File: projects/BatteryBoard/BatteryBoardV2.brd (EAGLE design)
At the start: 86.8 x 90.4 mm, 187 parts, among them M1 BSO201SP, SW1 BTS50015-1TAD, SW2 BTS50015-1TAD, U1 LTC4412MPS6, U3 LTC4121-4.2, U4 LTC4121-4.2, U5 LTC4121, U6 LTC4121

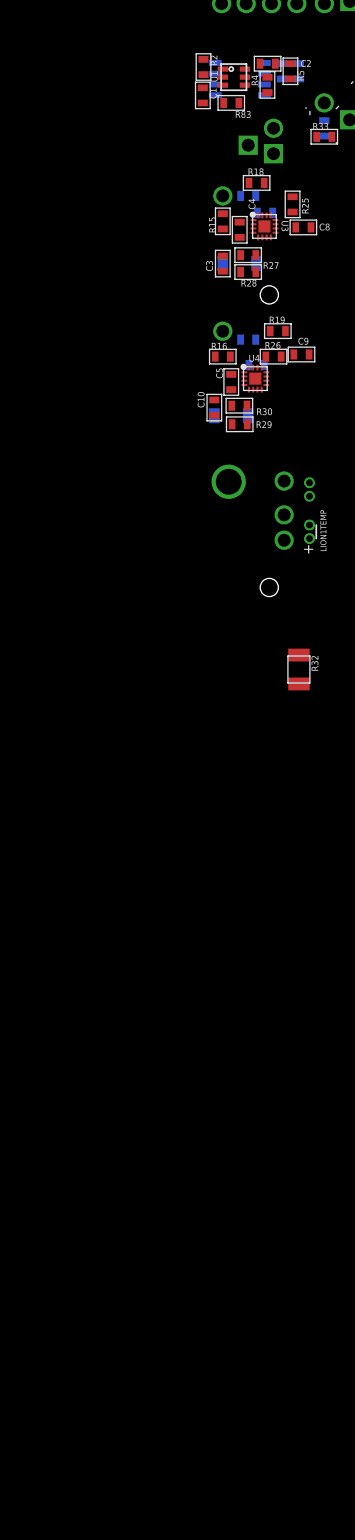
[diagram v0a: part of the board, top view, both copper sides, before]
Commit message: Finished programmer board and added output files to repo. Addiong of LDOs and continued fixes and updates to battery board v2.
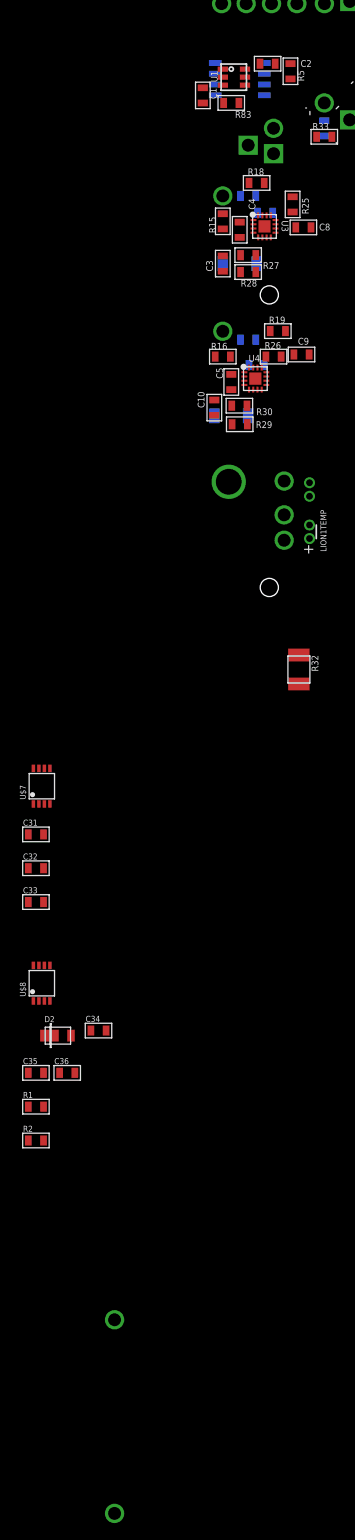
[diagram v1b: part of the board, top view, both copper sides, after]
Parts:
- removed R11: 10R, BrownSpaceEngineering:0805
- removed R12, R4: 0R, BrownSpaceEngineering:0805
- added C31, C34: 10uF, BrownSpaceEngineering:0805
- added C32, C35: 0.01uF, BrownSpaceEngineering:0805
- added C33, C36: 1uF, BrownSpaceEngineering:0805
- added D2: DFLS130L, BrownSpaceEngineering:PWRDI-123
- added R1: 1M, BrownSpaceEngineering:0805
- added U$7, U$8: LT1962-3, BrownSpaceEngineering:MSOP-8
- added V7, V8: (no value), BrownSpaceEngineering:VIA-60MIL
- D1: value (none) -> DFLS130L
- R2: value 0R -> 1M
- R84: value 1K -> 10K
- moved R2 128.5 mm to (-116.5, -63.4), turned to 0 degrees
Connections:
- removed net SP_C_O: R11.1, R12.1, R4.2, R5.2
- new net N$14: R2.2, U4.P$11
- new net N$3: C34.1, C35.1, D2.A, U$8.P$1, U$8.P$2
- new net N$4: C32.2, U$7.P$3
- new net N$6: R1.2, U3.P$11
- net GND: now also C31.2, C33.2, C34.2, C36.2, R1.1, R2.1, U$7.P$4, U$7.P$6, U$7.P$7, U$8.P$4, U$8.P$6, U$8.P$7; no longer R31.P$1
- net L_OUT: now also D1.C, D2.C
- net N$2: now also C31.1, C32.1, D1.A, U$7.P$1, U$7.P$2; no longer C2.1, M1.P$1, M1.P$2, M1.P$3, R4.1, U1.P$6
- net N$5: now also C35.2, U$8.P$3; no longer C1.1, M1.P$5, M1.P$6, M1.P$7, M1.P$8, R2.2, U1.P$1
- net SP_C: now also C1.1, M1.P$5, M1.P$6, M1.P$7, M1.P$8, U1.P$1; no longer R2.1
- net SP_OUT: now also C2.1, C33.1, C36.1, M1.P$1, M1.P$2, M1.P$3, R5.2, U$7.P$5, U$7.P$8, U$8.P$5, U$8.P$8, U1.P$6; no longer R11.2, R12.2

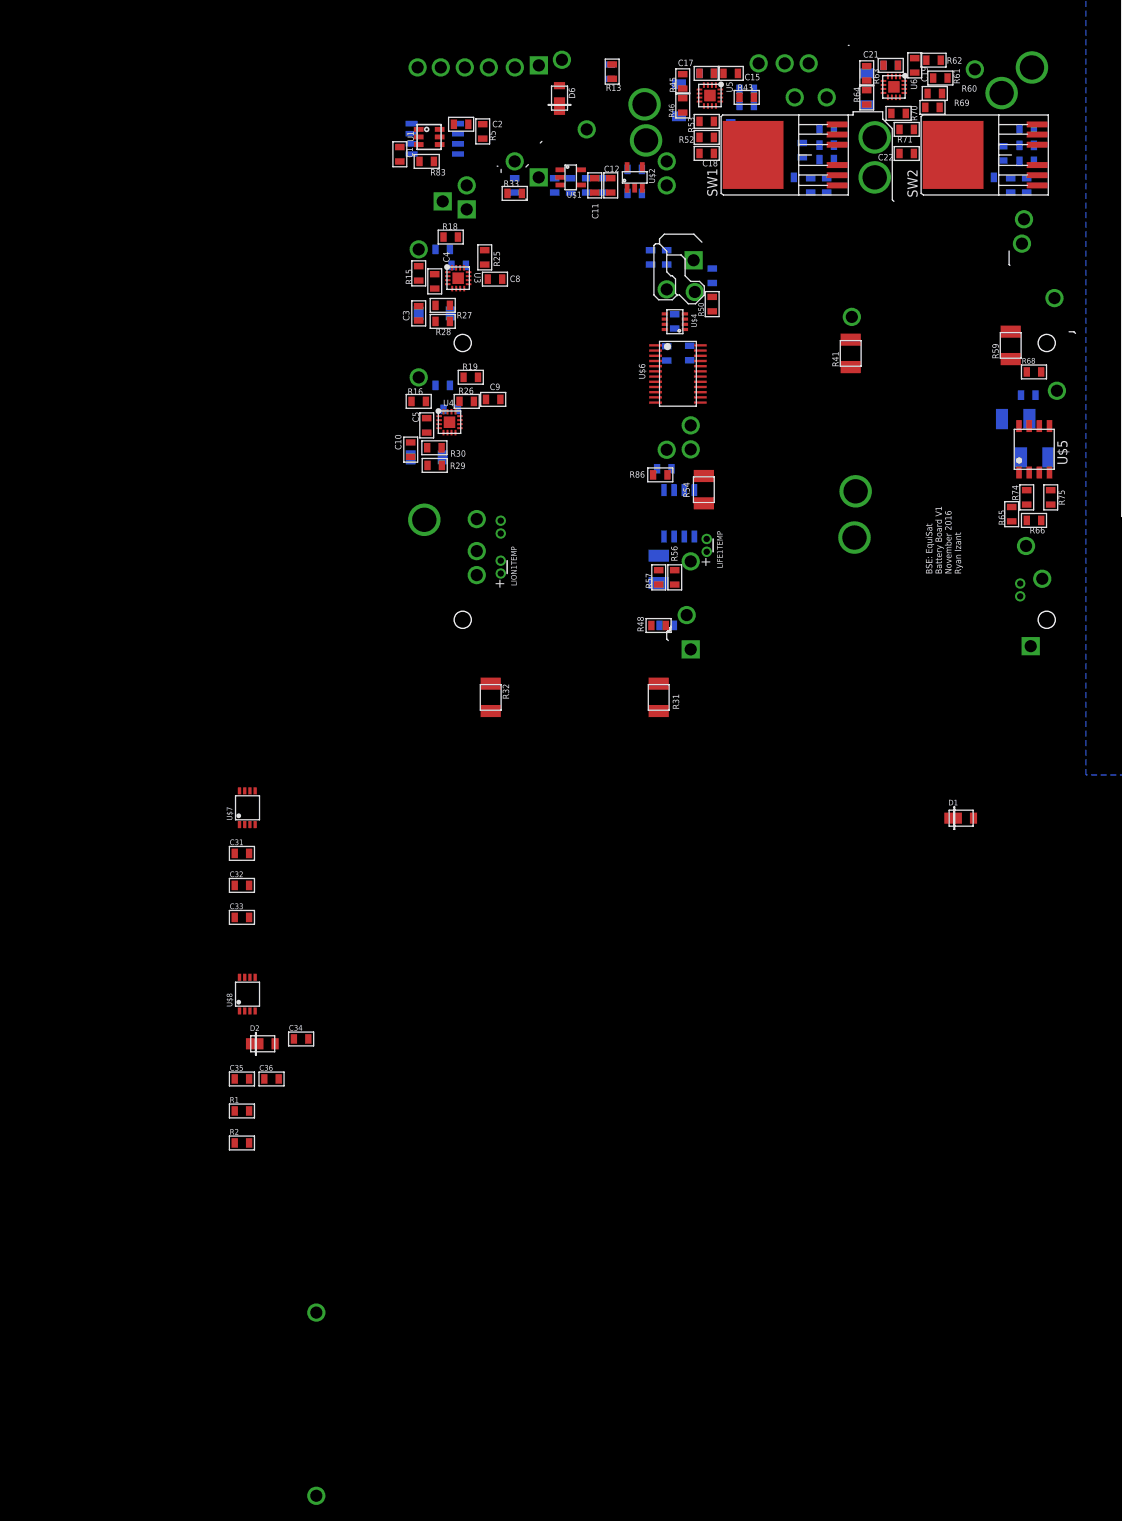
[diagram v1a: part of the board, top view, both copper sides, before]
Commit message: Continued addition of changes to battery board v2. Small updates to library including some part descriptions.
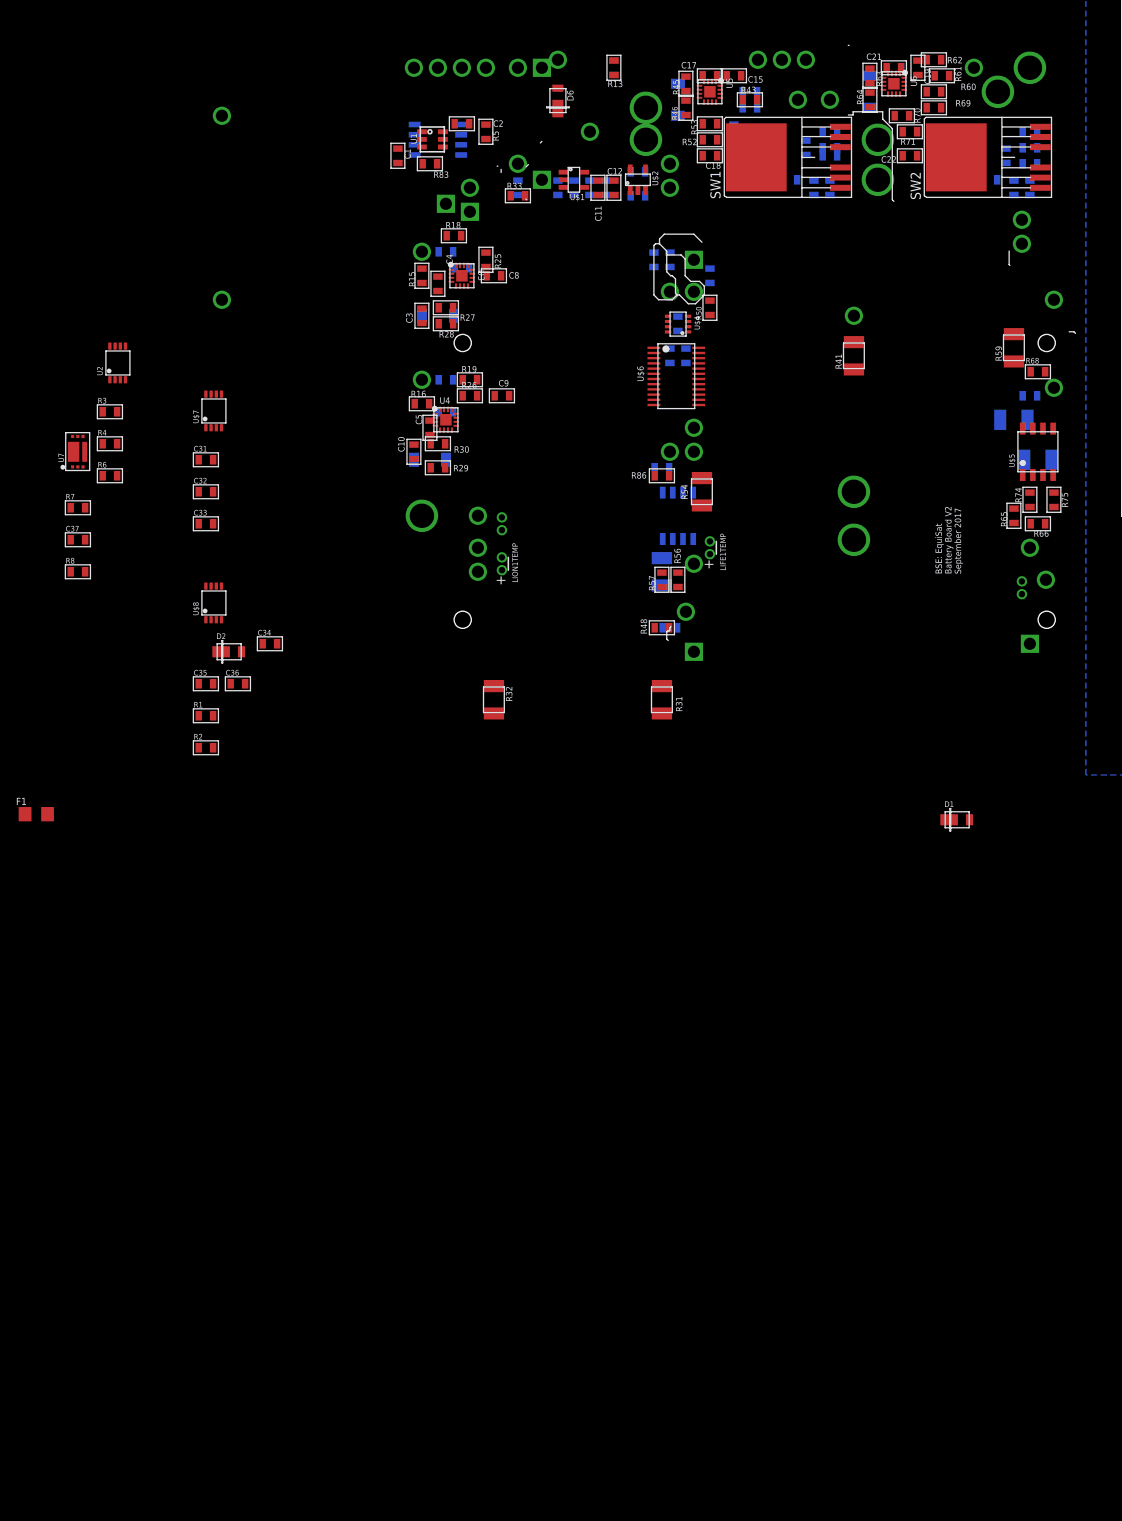
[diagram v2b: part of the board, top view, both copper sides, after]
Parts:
- added C37: 0.1uF, BrownSpaceEngineering:0805
- added F1: 1206L150THWR, BrownSpaceEngineering:1206
- added R3: 1M, BrownSpaceEngineering:0805
- added R4: 220K, BrownSpaceEngineering:0805
- added R6: 100K, BrownSpaceEngineering:0805
- added R7: 680R, BrownSpaceEngineering:0805
- added R8: 1K, BrownSpaceEngineering:0805
- added U2: AD8418, BrownSpaceEngineering:MSOP-8
- added U7: LC05111C13MTTTG, BrownSpaceEngineering:WDFN6
- R17, R18: value 10K -> 470K
- V7: value (none) -> LION1_GND+
- V8: value (none) -> LION1_GND-
- moved V7 150.1 mm to (-119.0, 65.0)
- moved V8 150.0 mm to (-119.0, 42.0)
- moved U$7 49.8 mm to (-121.0, 26.0)
- moved C35 49.6 mm to (-121.0, -6.00)
- moved R1 49.6 mm to (-121.0, -10.0)
- moved R2 49.6 mm to (-121.0, -14.0)
- moved C36 49.6 mm to (-117.0, -6.00)
- moved C34 49.6 mm to (-113.0, -1.00)
- moved C31 49.4 mm to (-121.0, 22.0)
- moved C32 49.4 mm to (-121.0, 18.0)
- moved C33 49.4 mm to (-121.0, 14.0)
- moved D2 49.2 mm to (-118.0, -2.00)
- moved U$8 49.1 mm to (-121.0, 2.00)
- moved C9 1.18 mm to (-84.0, 30.0)
- moved R20 0.81 mm to (-91.0, 32.0)
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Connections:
- removed net 3V3: C29.1, C30.1, R17.2, R18.2, R19.2, R20.2, R42.2, R43.2, R60.2, R61.2, R83.2, R84.2, R85.2, R86.2, U$4.P$8, U$6.P$24, V51.P$1
- new net +3V3: C29.1, C30.1, R17.2, R18.2, R19.2, R20.2, R4.1, R42.2, R43.2, R60.2, R61.2, R83.2, R84.2, R85.2, R86.2, U$4.P$8, U$6.P$24, U2.P$6, V51.P$1
- new net L1_SNS+: LI-ION1.MINUS, R31.P$2, U2.P$8
- new net N$15: R31.P$1, U2.P$1, V7.P$1
- new net N$16: U7.P$6, V8.P$1
- new net N$17: R3.1, U2.P$4
- new net N$34: R4.2, R6.1, U2.P$3, U2.P$7
- new net N$44: C37.2, R7.1, U7.P$5
- new net N$45: R8.2, U7.P$2
- new net N$46: F1.2, V45.P$1
- net GND: now also C37.1, R3.2, R6.2, R8.1, U2.P$2, U7.P$1, U7.P$3, U7.P$4
- net L1_SNS: now also U2.P$5; no longer LI-ION1.MINUS, R31.P$2
- net LION1: now also F1.1, R7.2; no longer V45.P$1
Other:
- board text added: "BSE: EquiSat Battery Board V2 September 2017"
- board text removed: "BSE: EquiSat Battery Board V1 November 2016 Ryan Izant"

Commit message: Continued improvements to the Battery Board schematic. Board reshaped.
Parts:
- removed D6: DFLS130L, BrownSpaceEngineering:PWRDI-123
- removed LIFEPO1, LIFEPO3: ~3.5V, BrownSpaceEngineering:EQUISAT-BATTERY-VA
- removed LIFEPO2, LIFEPO4: ~3.5V, BrownSpaceEngineering:EQUISAT-BATTERY-VB
- removed R26: 12.1K, BrownSpaceEngineering:0805
- removed R29: 43K, BrownSpaceEngineering:0805
- removed R30: 330K, BrownSpaceEngineering:0805
- removed R32: 0.13R@1W, BrownSpaceEngineering:1210
- removed R35: 150K, BrownSpaceEngineering:0805
- removed R36: 100K, BrownSpaceEngineering:0805
- removed U$4: AD7991-0, BrownSpaceEngineering:SOT-23-8
- removed U$6: TCA9535PWR, BrownSpaceEngineering:TSSOP-24
- removed V54: L_OUT, BrownSpaceEngineering:VIA-120MIL
- removed V56: LF_B2_OUTEN, BrownSpaceEngineering:VIA-60MIL
- removed V58: LF1_REF, BrownSpaceEngineering:VIA-60MIL
- removed V59: LF2_REF, BrownSpaceEngineering:VIA-60MIL
- removed V61: LF4_REF, BrownSpaceEngineering:VIA-60MIL
- removed V62: LF3_REF, BrownSpaceEngineering:VIA-60MIL
- added C38: 10nF, BrownSpaceEngineering:0805
- added D3: DFLS130L, BrownSpaceEngineering:PWRDI-123
- added F2: 1206L200, BrownSpaceEngineering:1206
- added LIFEPO41, LIFEPO43: ~3.5V, BrownSpaceEngineering:EQUISAT-BATTERY-VA
- added LIFEPO42, LIFEPO44: ~3.5V, BrownSpaceEngineering:EQUISAT-BATTERY-VB
- added R10: 330K, BrownSpaceEngineering:0805
- added R11: 43K, BrownSpaceEngineering:0805
- added R12: 0.13R@1W, BrownSpaceEngineering:1210
- added R21: 100K, BrownSpaceEngineering:0805
- added R22: 680R, BrownSpaceEngineering:0805
- added R23: 1K, BrownSpaceEngineering:0805
- added R9: 12.1K, BrownSpaceEngineering:0805
- added U14, U16: LTC4121, BrownSpaceEngineering:QFN-16-PAD
- added U8, U9: AD8418, BrownSpaceEngineering:MSOP-8
- added V11: LF3_TEMP, BrownSpaceEngineering:VIA-60MIL
- added V39: LIFE2, BrownSpaceEngineering:VIA-60MIL-SQ
- added V40: LIFEB1SNS, BrownSpaceEngineering:VIA-60MIL
- added V43: LF_B1_OUTEN, BrownSpaceEngineering:VIA-60MIL
- added V44: LF_B1, BrownSpaceEngineering:VIA-120MIL
- added V46: LF_B1_OSNS, BrownSpaceEngineering:VIA-60MIL
- C10, C34: value 10uF -> 22nF
- C11, C12: value 4.7uF -> 22uF
- C13, C14: value 1uF -> 0.1uF
- C15: value 2.2uF -> 1uF
- C16: value 22nF -> 1uF
- C17: value 10uF -> 1uF
- C18: value 22uF -> 1uF
- C19: value 2.2uF -> 0.01uF
- C20: value 22nF -> 0.01uF
- C21: value 10uF -> 4.7uF
- C22: value 22uF -> 4.7uF
- C23, C24: value 10nF -> 10uF
- C25: value 150nF -> 10uF
- C26: value 10nF -> 2.2uF
- C27: value 10nF -> 22nF
- C28: value 150nF -> 22uF
- C29: value 0.1uF -> 150nF
- C3: value 10uF -> 0.1uF
- C30, C37: value 0.1uF -> 10nF
- C31: value 10uF -> 10nF
- C32: value 0.01uF -> 10uF
- C33: value 1uF -> 2.2uF
- C35: value 0.01uF -> 22uF
- C36: value 1uF -> 150nF
- C4: value 22nF -> 0.1uF
- C5: value 22nF -> 10uF
- C6: value 2.2uF -> 10uF
- C8: value 22uF -> 2.2uF
- C9: value 22uF -> 22nF
- F1: value 1206L150THWR -> 1206L200
- R1: value 1M -> 10K
- R16: value 10K -> 150K
- R19: value 10K -> 100K
- R2, R3: value 1M -> 470K
- R20: value 10K -> 220K
- U1: value LTC4412MPS6 -> TCA9535PWR; device BrownSpaceEngineering:TSOT23-6 -> BrownSpaceEngineering:TSSOP-24
- U2: value AD8418 -> AD7991-0; device BrownSpaceEngineering:MSOP-8 -> BrownSpaceEngineering:SOT-23-8
- U3: value LTC4121-4.2 -> LTC4412MPS6; device BrownSpaceEngineering:QFN-16-PAD -> BrownSpaceEngineering:TSOT23-6
- U5: value LTC4121 -> LTC4121-4.2
- U6: value LTC4121 -> LC05111C13MTTTG; device BrownSpaceEngineering:QFN-16-PAD -> BrownSpaceEngineering:WDFN6
- V1: value UMB_CHG -> GND; device BrownSpaceEngineering:VIA-60MIL -> BrownSpaceEngineering:VIA-120MIL
- V10: value L1_CHG -> LF1_TEMP
- V12: value GND -> 3V3; device BrownSpaceEngineering:VIA-60MIL-SQ -> BrownSpaceEngineering:VIA-60MIL
- V13: value GND -> X_P; device BrownSpaceEngineering:VIA-120MIL -> BrownSpaceEngineering:VIA-60MIL
- V14: value LIFEB1SNS -> X_P; device BrownSpaceEngineering:VIA-60MIL -> BrownSpaceEngineering:VIA-60MIL-SQ
- V15: value LF_B1_CHG -> X_N
- V16: value LIFE2 -> Z_P; device BrownSpaceEngineering:VIA-60MIL-SQ -> BrownSpaceEngineering:VIA-60MIL
- V17: value LIFE1 -> Z_N; device BrownSpaceEngineering:VIA-60MIL-SQ -> BrownSpaceEngineering:VIA-60MIL
- V18: value LF_B1_CHGN -> Y_N
- V19: value LF_B1_FAULTN -> UMB_CHG
- V2: value X_P -> GND; device BrownSpaceEngineering:VIA-60MIL -> BrownSpaceEngineering:VIA-120MIL
- V20: value LF_B1_OUTEN -> L1_CHG
- V21: value LF_B1 -> L1_REF; device BrownSpaceEngineering:VIA-120MIL -> BrownSpaceEngineering:VIA-60MIL
- V22: value GND -> LION1_GND+; device BrownSpaceEngineering:VIA-120MIL -> BrownSpaceEngineering:VIA-60MIL
- V23: value GND -> LION1_GND-; device BrownSpaceEngineering:VIA-120MIL -> BrownSpaceEngineering:VIA-60MIL
- V24: value L1_TEMP -> LION2_GND+
- V25: value L1_REF -> LION2_GND-
- V26: value LF_B1 -> L1_FAULTN; device BrownSpaceEngineering:VIA-120MIL -> BrownSpaceEngineering:VIA-60MIL-SQ
- V27: value LIFE_B2 -> L1_CHGN; device BrownSpaceEngineering:VIA-120MIL -> BrownSpaceEngineering:VIA-60MIL-SQ
- V28: value LIFE_B2 -> LION1_OUT; device BrownSpaceEngineering:VIA-120MIL -> BrownSpaceEngineering:VIA-60MIL-SQ
- V29: value L2_REF -> L1_DISG
- V3: value X_N -> GND; device BrownSpaceEngineering:VIA-60MIL -> BrownSpaceEngineering:VIA-60MIL-SQ
- V30: value L_OUT -> L2_DISG; device BrownSpaceEngineering:VIA-120MIL -> BrownSpaceEngineering:VIA-60MIL
- V31: value LF_B1_OSNS -> L1_ST
- V32: value L2_TEMP -> L2_ST
- V33: value L2_CHG -> L_OUT; device BrownSpaceEngineering:VIA-60MIL -> BrownSpaceEngineering:VIA-120MIL
- V34: value L1_DISG -> L_OUT; device BrownSpaceEngineering:VIA-60MIL -> BrownSpaceEngineering:VIA-120MIL
- V35: value L2_DISG -> LF_B1_CHG
- V36: value L1_ST -> LF_B1_CHGN
- V37: value LF1_TEMP -> LF_B1_FAULTN
- V38: value L2_ST -> LIFE1; device BrownSpaceEngineering:VIA-60MIL -> BrownSpaceEngineering:VIA-60MIL-SQ
- V4: value Z_P -> GND; device BrownSpaceEngineering:VIA-60MIL -> BrownSpaceEngineering:VIA-120MIL
- V41: value L1_FAULTN -> LF1_REF; device BrownSpaceEngineering:VIA-60MIL-SQ -> BrownSpaceEngineering:VIA-60MIL
- V42: value L1_CHGN -> LF2_REF; device BrownSpaceEngineering:VIA-60MIL-SQ -> BrownSpaceEngineering:VIA-60MIL
- V45: value LION1 -> LF_B1; device BrownSpaceEngineering:VIA-60MIL-SQ -> BrownSpaceEngineering:VIA-120MIL
- V49: value X_P -> LF3_REF; device BrownSpaceEngineering:VIA-60MIL-SQ -> BrownSpaceEngineering:VIA-60MIL
- V5: value Z_N -> SCL
- V50: value LF3_TEMP -> LF4_REF
- V51: value 3V3 -> LF_B2_OUTEN
- V52: value SCL -> LIFE_B2; device BrownSpaceEngineering:VIA-60MIL -> BrownSpaceEngineering:VIA-120MIL
- V53: value SDA -> LIFE_B2; device BrownSpaceEngineering:VIA-60MIL -> BrownSpaceEngineering:VIA-120MIL
- V6: value Y_N -> SDA
- V7: value LION1_GND+ -> 5V
- V8: value LION1_GND- -> L1_TEMP
- V9: value 5V -> L2_TEMP
- moved U5 229.9 mm to (-71.8, -161.5), turned to 0 degrees
- moved V25 227.4 mm to (-110.9, -170.2), turned to 0 degrees
- moved R19 219.5 mm to (-128.4, -183.7), turned to 0 degrees
- moved R20 218.3 mm to (-124.7, -183.7), flipped to the top, turned to 0 degrees
- moved C12 217.2 mm to (-56.1, -160.8), turned to 0 degrees
- moved C14 216.3 mm to (-52.4, -160.8), flipped to the top
- moved R16 216.1 mm to (-132.1, -183.7)
- moved R3 209.9 mm to (-41.3, -160.8)
- moved C6 207.9 mm to (-67.2, -160.8), flipped to the top, turned to 0 degrees
- moved C8 207.3 mm to (-59.8, -160.8), turned to 0 degrees
- moved U7 191.4 mm to (-91.5, -162.9)
- moved V24 187.1 mm to (-133.8, -170.2)
- moved C10 186.5 mm to (-63.5, -160.8), turned to 0 degrees
- moved L2 184.2 mm to (-82.6, -161.9), flipped to the top, turned to 0 degrees
- moved R1 167.2 mm to (-48.7, -160.8)
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- renumbered LIFE1TEMP to T3, LIFE3TEMP to T4, LION1TEMP to T1, LION2TEMP to T2, U$1 to U12, U$2 to U13, U$3 to U15, U$5 to U17, U$7 to U11, U$8 to U10, V57 to V47, V60 to V48, V63 to $6_188_$_2017-09-09_23-53-10
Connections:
- removed net N$10: C5.1, U4.P$2
- removed net N$11: C5.2, L2.P$1, U4.P$4
- removed net N$13 (its old number): C6.1, U3.P$1
- removed net N$15: R31.P$1, U2.P$1, V7.P$1
- removed net N$19: R25.2, U3.P$13
- removed net N$20: R26.2, U4.P$13
- removed net N$21: R29.2, R30.1, U4.P$6
- removed net N$23: L2.P$2, U4.P$8
- removed net N$46: F1.2, V45.P$1
- new net L1_PROG: R25.2, U4.P$13
- new net L1_SNS-: R31.P$1, U8.P$1, V22.P$1
- new net L2_PROG: R9.2, U5.P$13
- new net L2_SNS+: LI-ION2.MINUS, R12.P$2, U9.P$8
- new net L2_SNS-: R12.P$1, U9.P$1, V24.P$1
- new net LION1_OUT: C15.2, F1.2, U12.P$1, V28.P$1
- new net LION2_OUT: C16.2, F2.2, U13.P$1
- new net N$48: R10.1, R11.2, U5.P$6
- new net N$49: L2.P$2, U5.P$8
- new net N$51: R20.2, R21.1, U9.P$3, U9.P$7
- new net N$52: U7.P$6, V25.P$1
- new net N$53: R23.2, U7.P$2
- new net N$54: C14.2, R22.1, U7.P$5
- net !BATT_INT!: now also U1.P$1; no longer U$6.P$1
- net +3V3: now also C1.1, C2.1, R2.2, R20.1, R3.2, U1.P$24, U2.P$8, U8.P$6, U9.P$6, V12.P$1; no longer C29.1, C30.1, R19.2, R20.2, U$4.P$8, U$6.P$24, U2.P$6, V51.P$1
- net 5V: now also V7.P$1; no longer V9.P$1
- net GND: now also C16.1, C17.2, C21.2, C26.1, C28.2, C29.1, C32.1, C33.1, C35.2, C36.1, C37.2, C38.2, C4.2, C5.2, R11.1, R19.1, R21.2, R23.1, R9.1, U1.P$12, U1.P$21, U14.P$12, U14.P$17, U14.P$5, U14.P$7, U16.P$12, U16.P$17, U16.P$5, U16.P$7, U2.P$7, U3.P$2, U3.P$3, U4.P$11, U5.P$11, U6.P$1, U6.P$3, U6.P$4, U8.P$2, U8.P$4, U9.P$2, U9.P$4, V1.P$1, V2.P$1, V3.P$1, V4.P$1; no longer C10.2, C17.1, C19.1, C21.1, C26.2, C27.2, C28.1, C29.2, C33.2, C34.2, C36.2, C37.1, C9.2, R1.1, R2.1, R26.1, R29.1, R3.2, R32.P$1, R36.1, U$4.P$7, U$6.P$12, U$6.P$2, U$6.P$21, U$6.P$3, U2.P$2, U3.P$12, U3.P$17, U3.P$5, U3.P$7, U6.P$12, U6.P$17, U6.P$5, U6.P$7, V12.P$1, V13.P$1, V22.P$1, V23.P$1
- net L1_CHG: now also U4.P$16, V20.P$1; no longer U3.P$16, V10.P$1
- net L1_CHGN: now also U1.P$8, U4.P$14, V27.P$1; no longer U$6.P$8, U3.P$14, V42.P$1
- net L1_DISG: now also V29.P$1; no longer V34.P$1
- net L1_FAULTN: now also U1.P$9, U4.P$15, V26.P$1; no longer U$6.P$9, U3.P$15, V41.P$1
- net L1_REF: now also V21.P$1; no longer V25.P$1
- net L1_SNS: now also U2.P$4, U8.P$5; no longer U$4.P$4, U2.P$5
- net L1_SNS+: now also U8.P$8; no longer U2.P$8
- net L1_ST: now also U1.P$5, V31.P$1; no longer U$6.P$5, V36.P$1
- net L1_TEMP: now also V8.P$1; no longer V24.P$1
- net L2_CHG: now also R1.2, U5.P$16; no longer R16.2, U4.P$16, V33.P$1
- net L2_CHGN: now also R2.1, U1.P$10, U5.P$14; no longer R19.1, U$6.P$10, U4.P$14
- net L2_DISG: now also V30.P$1; no longer V35.P$1
- net L2_FAULTN: now also R3.1, U1.P$11, U5.P$15; no longer R20.1, U$6.P$11, U4.P$15
- net L2_REF: now also R16.1, R19.2; no longer R35.1, R36.2, V29.P$1
- net L2_SNS: now also U2.P$3, U9.P$5; no longer LI-ION2.MINUS, R32.P$2, U$4.P$3
- net L2_ST: now also U1.P$4, V32.P$1; no longer U$6.P$4, V38.P$1
- net L2_TEMP: now also V9.P$1; no longer V32.P$1
- net LF1_REF: now also V41.P$1; no longer V58.P$1
- net LF1_TEMP: now also V10.P$1; no longer V37.P$1
- net LF2_REF: now also V42.P$1; no longer V59.P$1
- net LF3_REF: now also V49.P$1; no longer V62.P$1
- net LF3_TEMP: now also V11.P$1; no longer V50.P$1
- net LF4_REF: now also V50.P$1; no longer V61.P$1
- net LF_B1: now also C30.1, V44.P$1, V45.P$1; no longer C23.1, V21.P$1, V26.P$1
- net LF_B1_BT: now also U1.P$13; no longer U$6.P$13
- net LF_B1_CHG: now also U14.P$16, V35.P$1; no longer U5.P$16, V15.P$1
- net LF_B1_CHGN: now also U1.P$19, U14.P$14, V36.P$1; no longer U$6.P$19, U5.P$14, V18.P$1
- net LF_B1_FAULTN: now also U1.P$20, U14.P$15, V37.P$1; no longer U$6.P$20, U5.P$15, V19.P$1
- net LF_B1_OSNS: now also C31.1, V46.P$1; no longer C24.1, V31.P$1
- net LF_B1_OUTEN: now also V43.P$1; no longer V20.P$1
- net LF_B1_TT: now also U1.P$14; no longer U$6.P$14
- net LF_B2_BT: now also U1.P$16; no longer U$6.P$16
- net LF_B2_CHG: now also U16.P$16; no longer U6.P$16
- net LF_B2_CHGN: now also U1.P$17, U16.P$14; no longer U$6.P$17, U6.P$14
- net LF_B2_FAULTN: now also U1.P$18, U16.P$15; no longer U$6.P$18, U6.P$15
- net LF_B2_OSNS: now also C38.1; no longer C27.1
- net LF_B2_OUTEN: now also V51.P$1; no longer V56.P$1
- net LF_B2_SNS: now also LIFEPO44.MINUS; no longer LIFEPO4.MINUS
- net LF_B2_TT: now also U1.P$15; no longer U$6.P$15
- net LIFE1: now also C28.1, LIFEPO41.PLUS, U14.P$9, V38.P$1; no longer C18.1, LIFEPO1.PLUS, U5.P$9, V17.P$1
- net LIFE2: now also LIFEPO41.MINUS, LIFEPO42.PLUS, V39.P$1; no longer LIFEPO1.MINUS, LIFEPO2.PLUS, V16.P$1
- net LIFE3: now also C35.1, LIFEPO43.PLUS, U16.P$9; no longer C22.1, LIFEPO3.PLUS, U6.P$9
- net LIFE4: now also LIFEPO43.MINUS, LIFEPO44.PLUS; no longer LIFEPO3.MINUS, LIFEPO4.PLUS
- net LIFEB1SNS: now also LIFEPO42.MINUS, V40.P$1; no longer LIFEPO2.MINUS, V14.P$1
- net LIFE_B2: now also C37.1, V52.P$1, V53.P$1; no longer C26.1, V27.P$1, V28.P$1
- net LION1: now also C11.1, U4.P$10, U4.P$9; no longer C13.2, C8.1, U12.P$1, U3.P$10, U3.P$9
- net LION2: now also C12.1, F2.1, R16.2, R22.2, U5.P$10, U5.P$9; no longer C14.2, C9.1, R35.2, U13.P$1, U4.P$10, U4.P$9
- net L_OUT: now also C21.1, C22.1, D3.C, V33.P$1, V34.P$1; no longer C11.1, C12.1, D1.C, V30.P$1, V54.P$1
- net L_REF: now also U2.P$5; no longer U$4.P$5
- net N$1: now also U3.P$5; no longer U1.P$5
- net N$1356: now also C36.2; no longer C28.2
- net N$14: now also C10.1, U5.P$2; no longer R2.2, U4.P$11
- net N$16: now also U6.P$6, V23.P$1; no longer U7.P$6, V8.P$1
- net N$17: now also C8.1, U5.P$1; no longer R3.1, U2.P$4
- net N$18: now also U4.P$8; no longer U3.P$8
- net N$2: now also C20.1, C24.1, D3.A; no longer C31.1, C32.1, D1.A
- net N$22: now also U4.P$6; no longer U3.P$6
- net N$26: now also U14.P$11; no longer U5.P$11
- net N$27: now also U14.P$6; no longer U5.P$6
- net N$28: now also U14.P$10; no longer U5.P$10
- net N$29: now also C26.2, U14.P$1; no longer C15.2, U5.P$1
- net N$3: now also C19.1, C23.1; no longer C34.1, C35.1
- net N$30: now also C27.1, U14.P$4; no longer C16.1, U5.P$4
- net N$31: now also C27.2, U14.P$2; no longer C16.2, U5.P$2
- net N$32: now also U14.P$8; no longer U5.P$8
- net N$33: now also U16.P$6; no longer U6.P$6
- net N$34: now also U8.P$3, U8.P$7; no longer U2.P$3, U2.P$7
- net N$35: now also U16.P$13; no longer U6.P$13
- net N$36: now also U16.P$11; no longer U6.P$11
- net N$37: now also U16.P$10; no longer U6.P$10
- net N$38: now also C33.2, U16.P$1; no longer C19.2, U6.P$1
- net N$39: now also C34.1, U16.P$4; no longer C20.1, U6.P$4
- net N$4: now also C20.2; no longer C32.2
- net N$40: now also C34.2, U16.P$2; no longer C20.2, U6.P$2
- net N$41: now also U16.P$8; no longer U6.P$8
- net N$44: now also C13.2, U6.P$5; no longer C37.2, U7.P$5
- net N$45: now also U6.P$2; no longer U7.P$2
- net N$5: now also C19.2; no longer C35.2
- net N$6: now also C10.2, L2.P$1, U5.P$4; no longer R1.2, U3.P$11
- net N$68: now also C29.2; no longer C25.2
- net N$7: now also U14.P$13; no longer U5.P$13
- net N$8: now also C9.2, U4.P$4; no longer C4.2, U3.P$4
- net N$9: now also C9.1, U4.P$2; no longer C4.1, U3.P$2
- net PANELREF: now also U2.P$6; no longer U$4.P$6
- net SCL: now also U1.P$22, U2.P$1, V5.P$1; no longer U$4.P$1, U$6.P$22, V52.P$1
- net SDA: now also U1.P$23, U2.P$2, V6.P$1; no longer U$4.P$2, U$6.P$23, V53.P$1
- net SPF_ST: now also U1.P$6, U3.P$4; no longer U$6.P$6, U1.P$4
- net SP_C: now also C3.1, U3.P$1, V13.P$1, V14.P$1, V15.P$1, V16.P$1, V17.P$1, V18.P$1; no longer C1.1, U1.P$1, V2.P$1, V3.P$1, V4.P$1, V49.P$1, V5.P$1, V6.P$1
- net SP_OUT: now also C17.1, C18.1, C25.2, C32.2, C4.1, C5.1, C6.1, D1.C, R1.1, R10.2, U14.P$3, U16.P$3, U3.P$6; no longer C10.1, C17.2, C2.1, C21.2, C3.1, C33.1, C36.1, D6.C, R16.1, R30.2, U1.P$6, U3.P$3, U6.P$3
- net UMB_CHG: now also D1.A, V19.P$1; no longer D6.A, V1.P$1
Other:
- board size 86.8 x 90.4 mm -> 90.5 x 96 mm

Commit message: Added #2 MTG part to BSE libary. Added 2016L PTC fuse part to BSE library. Adjusted BSE libary part descriptions. Added net classes, lifepo current sense and fusing, schematic clean up, mounting parts, and initial board layout for large components to Battery Board V2.
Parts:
- removed V40: LIFEB1SNS, BrownSpaceEngineering:VIA-60MIL
- removed V44: LF_B1, BrownSpaceEngineering:VIA-120MIL
- removed V48: LF_B2_SNS, BrownSpaceEngineering:VIA-60MIL
- removed V52: LIFE_B2, BrownSpaceEngineering:VIA-120MIL
- added F3, F4, F5, F6: 2016L500, BrownSpaceEngineering:2016
- added MTG1, MTG2, MTG3, MTG4: (no value), BrownSpaceEngineering:#2-CLOSE-NPTH
- added R24, R29: 220K, BrownSpaceEngineering:0805
- added R26, R30: 100K, BrownSpaceEngineering:0805
- added U18, U19: AD8418, BrownSpaceEngineering:MSOP-8
- moved C10 261.0 mm to (-50.3, 99.9)
- moved C12 261.0 mm to (-42.9, 99.9)
- moved C14 261.0 mm to (-39.2, 99.9)
- moved C6 261.0 mm to (-54.0, 99.9)
- moved C8 261.0 mm to (-46.6, 99.9)
- moved F2 261.0 mm to (-63.6, 98.9)
- moved R1 261.0 mm to (-35.5, 99.9)
- moved R2 261.0 mm to (-31.8, 99.9)
- moved R3 261.0 mm to (-28.1, 99.9)
- moved L2 261.0 mm to (-69.4, 98.8)
- moved R10 261.0 mm to (-126.3, 77.0)
- moved R11 261.0 mm to (-122.6, 77.0)
- moved R12 261.0 mm to (-83.6, 97.7)
- moved R16 261.0 mm to (-118.9, 77.0)
- moved R19 261.0 mm to (-115.2, 77.0)
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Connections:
- removed net LIFEB1SNS: LIFEPO42.MINUS, R41.P$2, V40.P$1
- new net LF_B1_SNS: U18.P$5
- new net LIFE1FUSEOUT: F3.P$2, F4.P$2, SW1.PAD
- new net LIFE3FUSEOUT: F5.P$2, F6.P$2, SW2.PAD
- new net N$10: R29.2, R30.1, U19.P$3, U19.P$7
- new net N$11: R24.2, R26.1, U18.P$3, U18.P$7
- net +3V3: now also R24.1, R29.1, U18.P$6, U19.P$6
- net GND: now also R26.2, R30.2, U18.P$1, U18.P$2, U18.P$4, U19.P$1, U19.P$2, U19.P$4
- net L1_SNS+: now also LIFEPO42.MINUS, LIFEPO44.MINUS, R41.P$2, R59.P$2, U18.P$8, U19.P$8
- net LF_B1: no longer V44.P$1
- net LF_B2_SNS: now also U19.P$5; no longer LIFEPO44.MINUS, R59.P$2, V48.P$1
- net LIFE1: now also F3.P$1, F4.P$1; no longer SW1.PAD
- net LIFE3: now also F5.P$1, F6.P$1; no longer SW2.PAD
- net LIFE_B2: no longer V52.P$1
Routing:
- added copper zone on layer 16, net LIFE1
- added copper zone on layer 16, net LIFE1FUSEOUT
- added copper zone on layer 16, net LIFE3
- added copper zone on layer 16, net LIFE3FUSEOUT
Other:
- outline, holes or cut-outs redrawn
